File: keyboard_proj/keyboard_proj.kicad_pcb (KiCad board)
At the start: 2 copper layers, 74 parts, among them IC1 DW01A-G, IC2 TP4056-42-ESOP8, IC3 LD1117DT12CTR, IC4 USBLC6-4SC6, J1 Conn_02x04_Odd_Even, J2 Conn_01x32, Q1 FS8205A, Q2 2N7002, SW1 SW_Push, U1 STM32WB55CGU6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

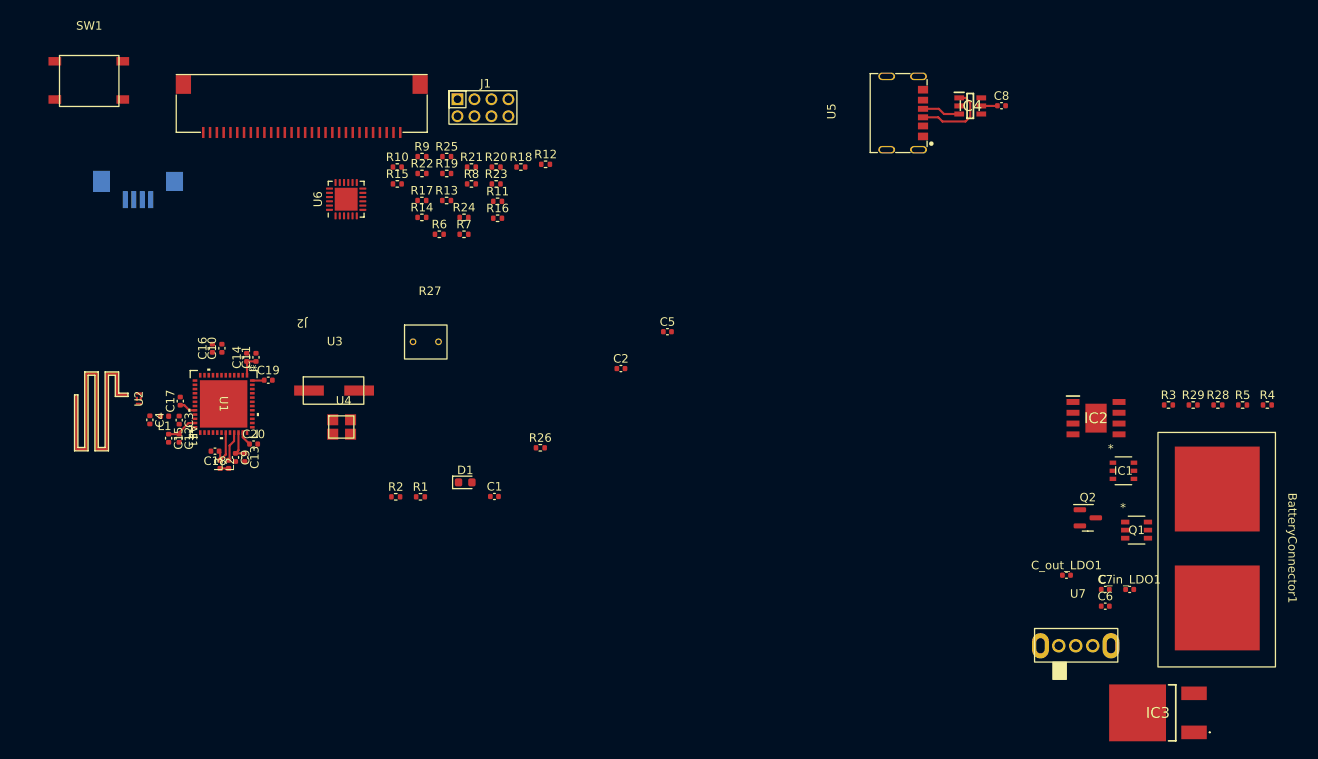
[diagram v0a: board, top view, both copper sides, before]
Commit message: passage kicad 7, routing bien avancé
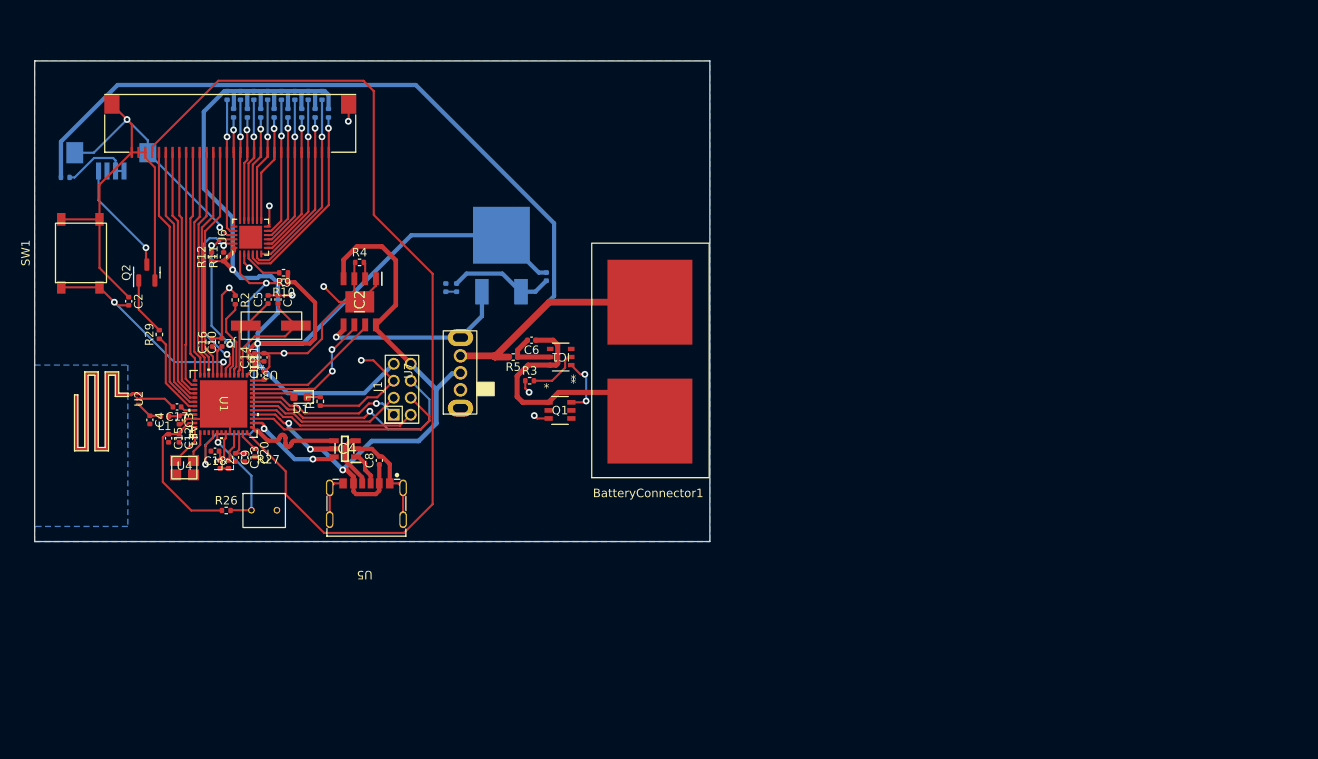
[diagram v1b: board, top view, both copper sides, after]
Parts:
- C7, C_in_LDO1, C_out_LDO1, IC3, R13, R14, R15, R16, R17, R18, R19, R20, R21, R22, R23, R24, R25, R28, R6, R7, R8: moved to B.Cu
- moved R28 138.3 mm to (64.1, 75.9)
- moved R29 122.0 mm to (75.1, 94.4), turned to 90 degrees
- moved Q2 114.5 mm to (73.7, 87.1), turned to 90 degrees
- moved R4 108.2 mm to (98.7, 85.9)
- moved IC3 94.0 mm to (115.4, 84.2), turned to -90 degrees
- moved IC2 87.8 mm to (98.7, 90.5), turned to -90 degrees
- moved C_in_LDO1 86.9 mm to (110.1, 88.9), turned to -90 degrees
- moved R5 86.1 mm to (116.8, 97.0), turned to 180 degrees
- moved C7 85.4 mm to (108.9, 88.9), turned to 90 degrees
- moved C8 84.3 mm to (101.0, 109.2), turned to 90 degrees
- moved IC4 84.0 mm to (97.0, 107.9), turned to 180 degrees
- moved U7 79.2 mm to (110.6, 98.9), turned to 90 degrees
- moved U5 78.2 mm to (99.5, 114.1), turned to 180 degrees
- moved R3 75.3 mm to (118.7, 99.8)
- moved C6 74.5 mm to (119.0, 95.1), turned to 180 degrees
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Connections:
- IC2 pad 5: /battery_mgmnt/Vbat+ -> /battery_mgmnt/+
- IC3 pad 3: /battery_mgmnt/Vbat+ -> /battery_mgmnt/+
- J2 pad 17: PA10 -> PA0
- J2 pad 18: PA9 -> PA1
- J2 pad 19: PA8 -> PA2
- J2 pad 20: PA7 -> PA3
- J2 pad 21: PA6 -> PA4
- J2 pad 23: PA4 -> PA6
- J2 pad 24: PA3 -> PA7
- J2 pad 25: PA2 -> PA8
- J2 pad 26: PA1 -> PA9
- J2 pad 27: PA0 -> PA10
- U7 pad 4: /battery_mgmnt/Vbat+ -> /battery_mgmnt/+
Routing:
- net GND: track 0.00 -> 176.3 mm, vias 0 -> 12
- net /Power/VDDA: track 15.3 -> 188.7 mm, vias 0 -> 2
- net /battery_mgmnt/+: track 0.00 -> 137.1 mm, vias 0 -> 1
- net PA10: track 0.00 -> 111.7 mm
- net /VBUS: track 1.91 -> 76.0 mm, vias 0 -> 3
- net //INT: track 0.00 -> 38.7 mm, vias 0 -> 2
- net PA9: track 0.00 -> 31.5 mm
- net PA8: track 0.00 -> 30.6 mm
- net /battery_mgmnt/-: track 0.00 -> 30.6 mm
- net PA7: track 0.00 -> 29.8 mm
- net PA6: track 0.00 -> 28.9 mm
- net /JTDO: track 0.00 -> 28.9 mm, vias 0 -> 1
- net PA5: track 0.00 -> 28.1 mm
- net PA0: track 0.00 -> 27.4 mm
- net PA4: track 0.00 -> 27.2 mm
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- added copper zone on B.Cu, net GND
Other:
- board outline added: 79.5 x 56.6 mm

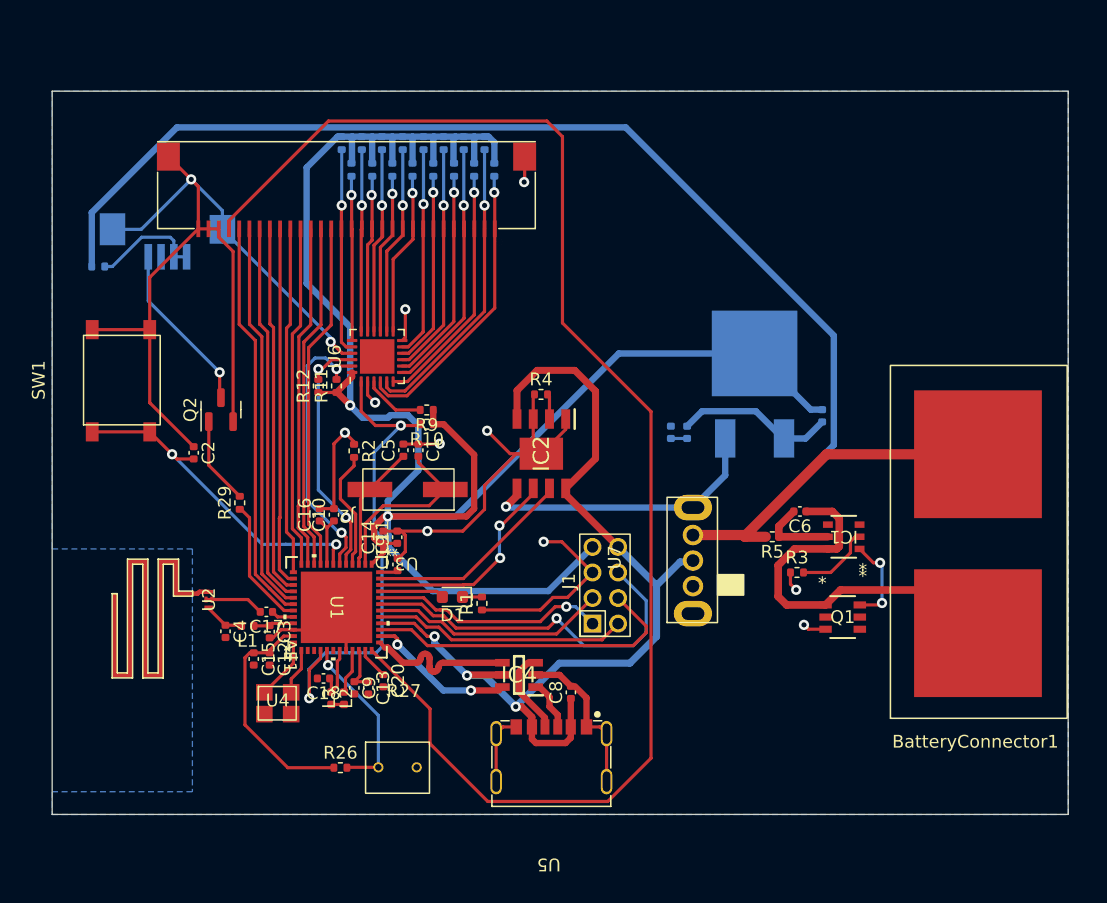
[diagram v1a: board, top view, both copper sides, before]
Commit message: Routing bientot fini check schematic et tout mettre sur la meme face
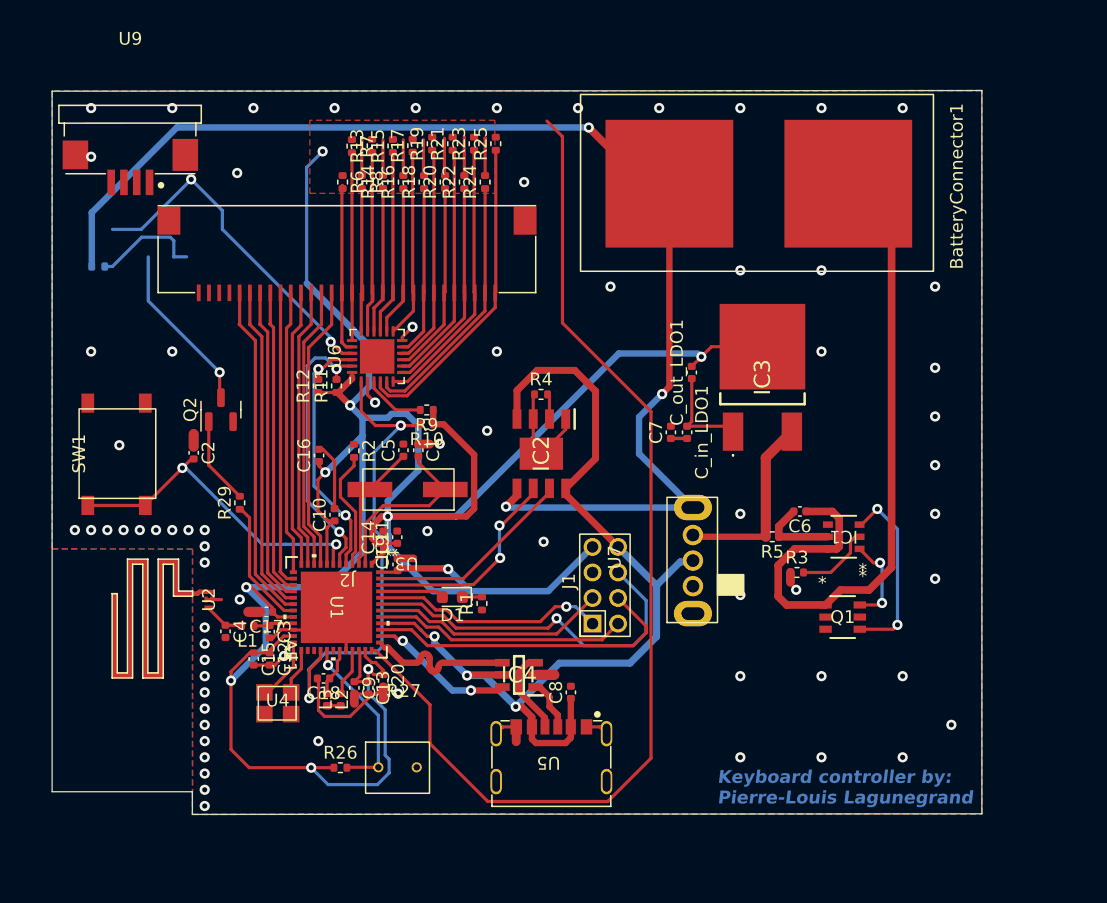
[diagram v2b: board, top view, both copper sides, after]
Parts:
- C7, C_in_LDO1, C_out_LDO1, IC3, R13, R14, R15, R16, R17, R18, R19, R20, R21, R22, R23, R24, R25, R6, R7, R8, U9: moved to F.Cu
- moved BatteryConnector1 33.0 mm to (115.7, 69.4), turned to 180 degrees
- moved C_out_LDO1 10.7 mm to (110.5, 84.2)
- moved U9 6.51 mm to (66.6, 68.2), turned to 0 degrees
- moved SW1 5.76 mm to (65.5, 90.6)
- moved J2 5.01 mm to (83.5, 74.4)
- moved C16 4.65 mm to (81.3, 90.7)
- moved R20 3.05 mm to (91.2, 69.3)
- moved R6 3.05 mm to (83.2, 69.3)
- moved R16 3.05 mm to (87.9, 69.3)
- moved R18 3.05 mm to (89.6, 69.3)
- moved R22 3.05 mm to (92.7, 69.3)
- moved R24 3.05 mm to (94.3, 69.3)
- moved R14 3.04 mm to (86.3, 69.3)
- moved R8 3.04 mm to (84.7, 69.3)
- moved R19 2.04 mm to (90.2, 66.3)
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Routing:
- net GND: track 176.3 -> 80.9 mm, vias 12 -> 73
- net /Power/VDDA: track 188.7 -> 246.2 mm, vias 2 -> 10
- net PA10: track 111.7 -> 83.2 mm
- net /battery_mgmnt/-: track 30.6 -> 54.6 mm
- net /battery_mgmnt/+: track 137.1 -> 113.3 mm, vias 1 -> 3
- net Net-(IC1-OC): track 0.00 -> 14.7 mm, vias 0 -> 2
- net PA2: track 27.0 -> 21.9 mm
- net PA5: track 28.1 -> 23.1 mm
- net PA8: track 30.6 -> 25.6 mm
- net PA9: track 31.5 -> 26.5 mm
- net PA7: track 29.8 -> 24.8 mm
- net PA6: track 28.9 -> 23.9 mm
- net PA4: track 27.2 -> 22.2 mm
- net PA3: track 26.8 -> 21.8 mm
- net PA1: track 27.1 -> 22.1 mm
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- added copper zone on F.Cu, net /Power/VDDA
- added copper zone on F.Cu, net GND
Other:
- board size 79.5 x 56.6 mm -> 72.7 x 56.6 mm
- board text added: "Keyboard controller by: Pierre-Louis Lagunegrand"

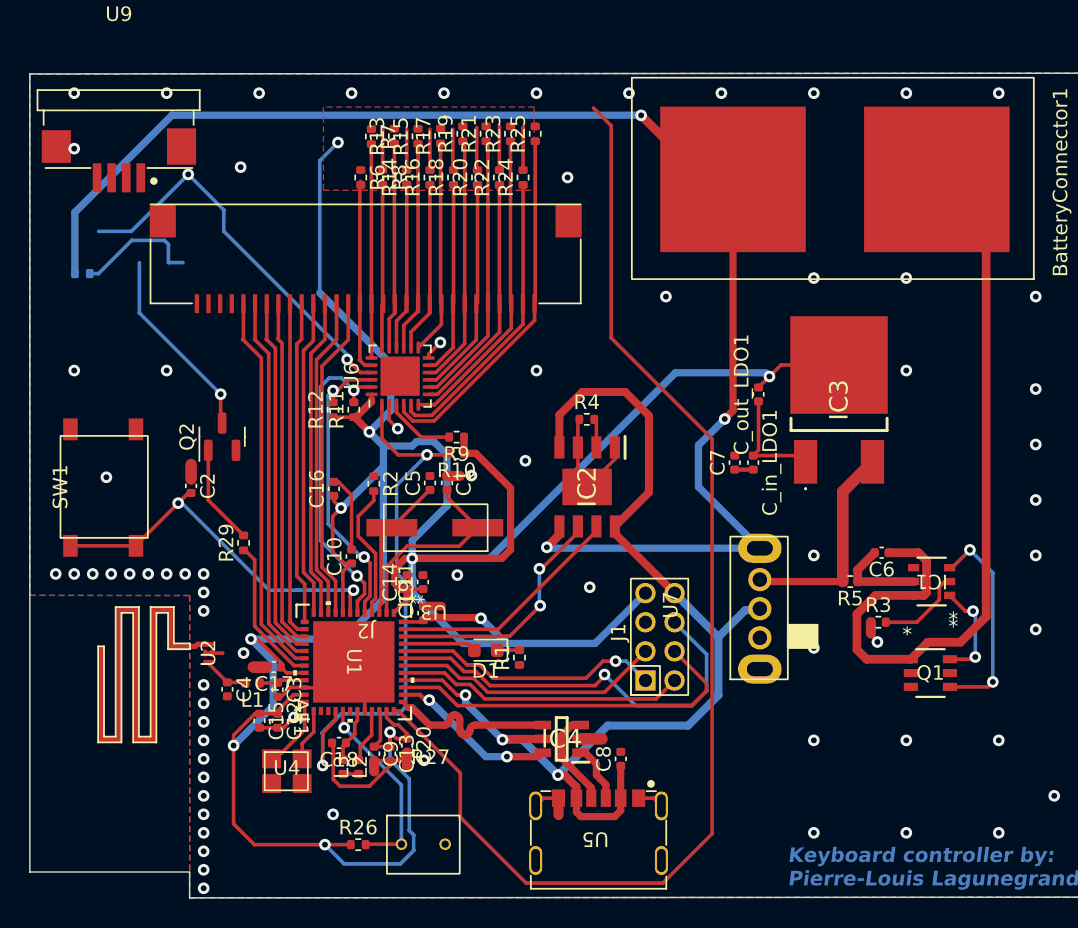
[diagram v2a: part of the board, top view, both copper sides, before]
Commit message: Power dlvry changée, ok mtn, routing updated
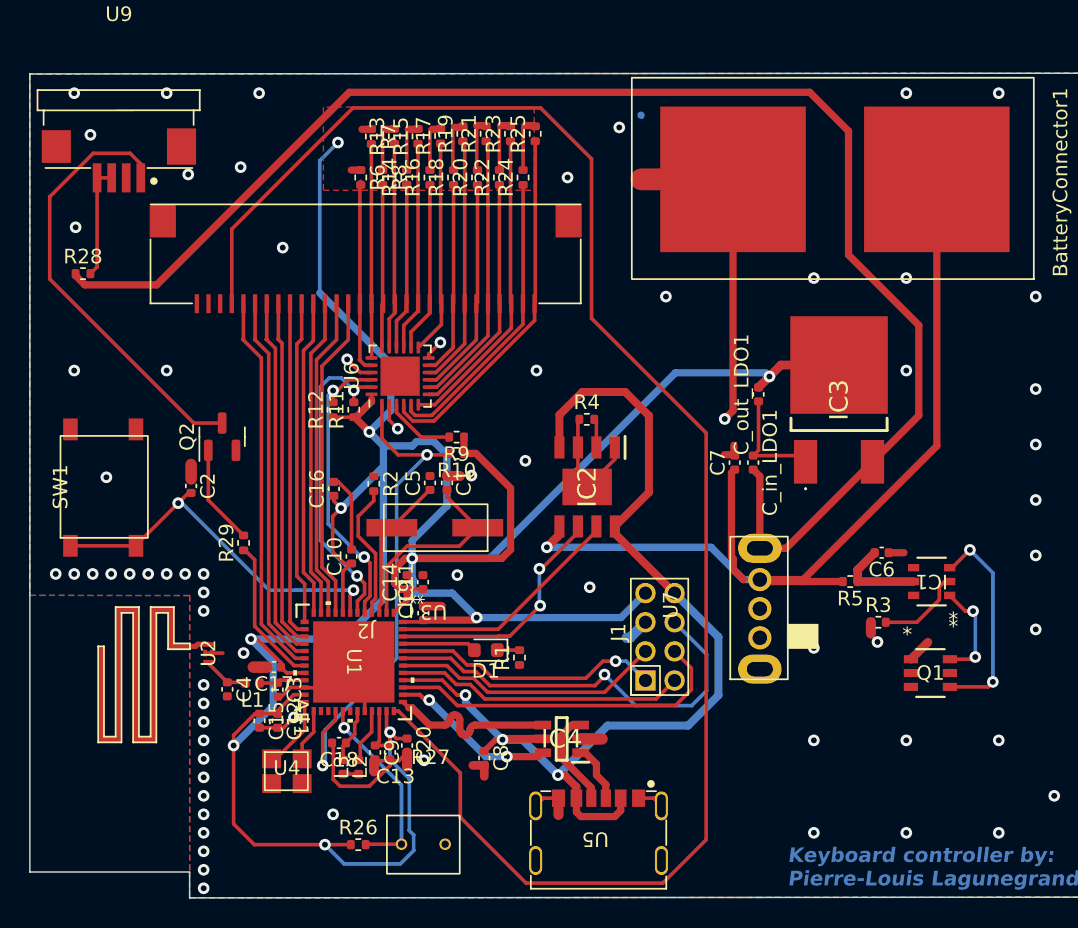
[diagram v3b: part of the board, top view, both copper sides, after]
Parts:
- R28: moved to F.Cu
- moved C8 9.38 mm to (91.7, 109.2), turned to -90 degrees
- moved C9 0.11 mm to (84.2, 108.8)
- moved C13 0.09 mm to (85.2, 108.8)
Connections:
- net /Power/VDDA renamed /Power/3.3V
- BatteryConnector1 pad 1: /battery_mgmnt/- -> /battery_mgmnt/Vbat+
- BatteryConnector1 pad 2: /battery_mgmnt/+ -> GND
- C6 pad 1: /battery_mgmnt/- -> GND
- C_in_LDO1 pad 2: /battery_mgmnt/Vbat+ -> /battery_mgmnt/sel_bat_out
- IC1 pad 6: /battery_mgmnt/- -> GND
- IC2 pad 5: /battery_mgmnt/+ -> /battery_mgmnt/Vbat+
- IC3 pad 3: /battery_mgmnt/+ -> /battery_mgmnt/sel_bat_out
- Q1 pad 1: /battery_mgmnt/- -> GND
- R28 pad 1: /battery_mgmnt/+ -> /battery_mgmnt/sel_bat_out
- R5 pad 2: /battery_mgmnt/+ -> /battery_mgmnt/Vbat+
- U7 pad 2: /VBUS -> unconnected-(U7-state1-Pad2)
- U7 pad 3: /battery_mgmnt/+ -> /battery_mgmnt/Vbat+
- U7 pad 4: /battery_mgmnt/+ -> /battery_mgmnt/sel_bat_out
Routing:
- net /battery_mgmnt/+: track 113.3 -> 0.00 mm, vias 3 -> 0
- net /battery_mgmnt/sel_bat_out: track 0.00 -> 101.9 mm
- net /battery_mgmnt/Vbat+: track 2.54 -> 66.6 mm, vias 0 -> 1
- net /battery_mgmnt/-: track 54.6 -> 0.00 mm
- net PA10: track 83.2 -> 114.1 mm
- net Net-(Q2-D): track 13.4 -> 30.5 mm, vias 1 -> 0
- net GND: track 80.9 -> 86.7 mm, vias 73 -> 70
- net /VBUS: track 76.0 -> 71.7 mm
- net //INT: track 38.7 -> 35.9 mm
- net /SWIO: track 25.4 -> 23.9 mm
- net Net-(R28-Pad2): track 8.72 -> 7.77 mm

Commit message: PCB bien avancé, presque fini mais je dois selectionner des pieces de jlcpcb pour baisser les couts
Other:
- board size 72.7 x 56.6 mm -> 72.9 x 56.6 mm
